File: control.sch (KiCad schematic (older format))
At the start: 17 parts, among them IC1 ATTINY4313-P, P2 CONN_02X03, SW1 SW_Push, Y1 11.0592MHz

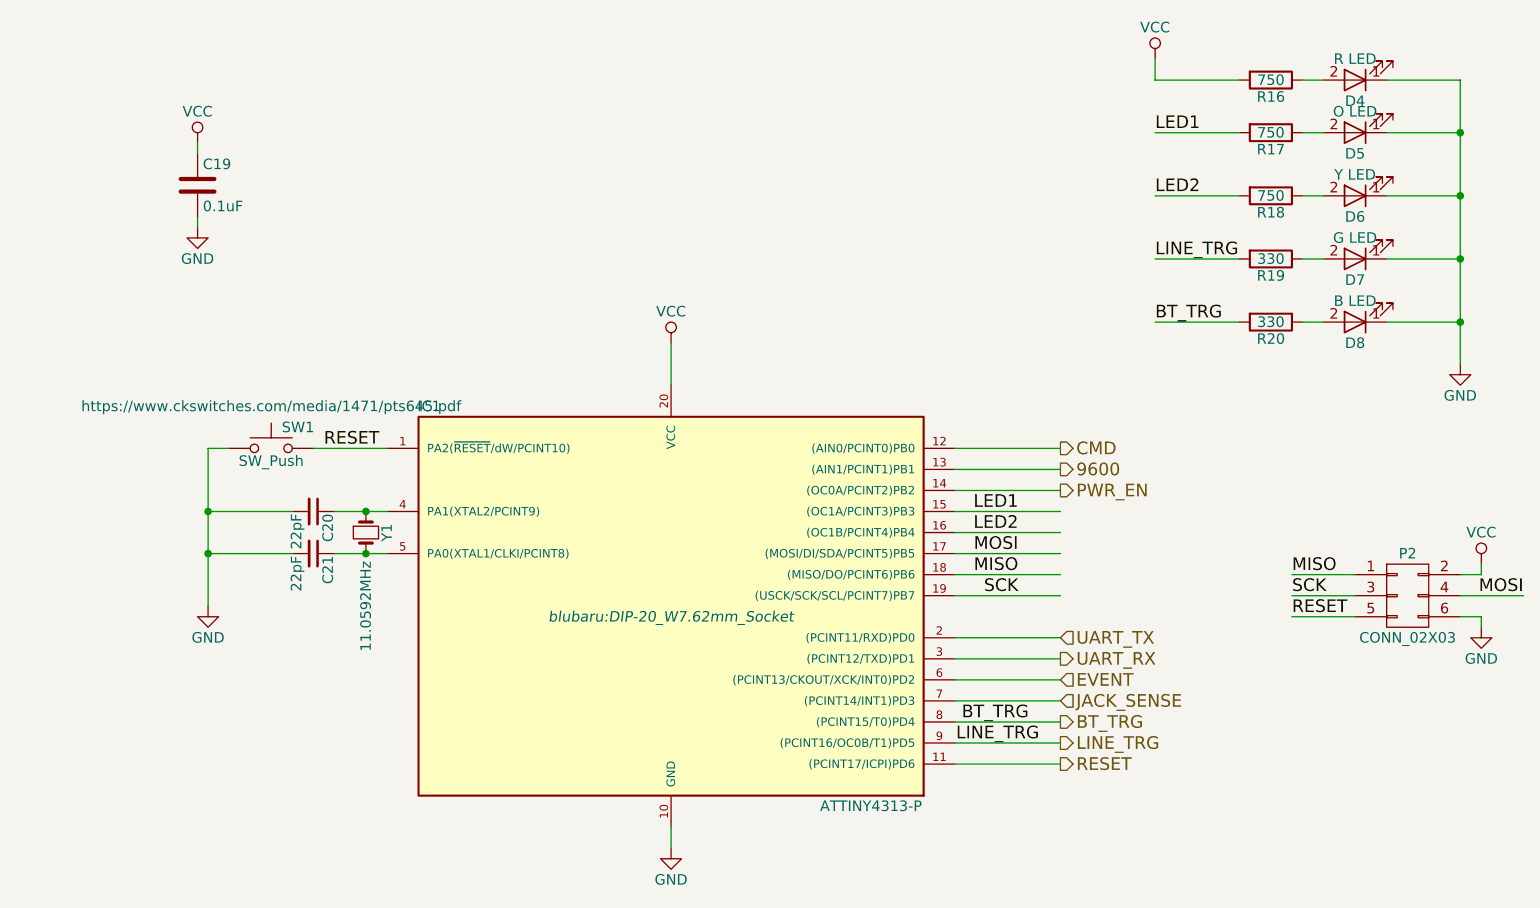
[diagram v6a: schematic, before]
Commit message: Rename the bluetooth reset line
This is needed so it doesn't conflict with the MCU reset line of the
same name. Apparently that puts them on the same net.

Also, reorder the LEDs so they have nicer numbers on the board.
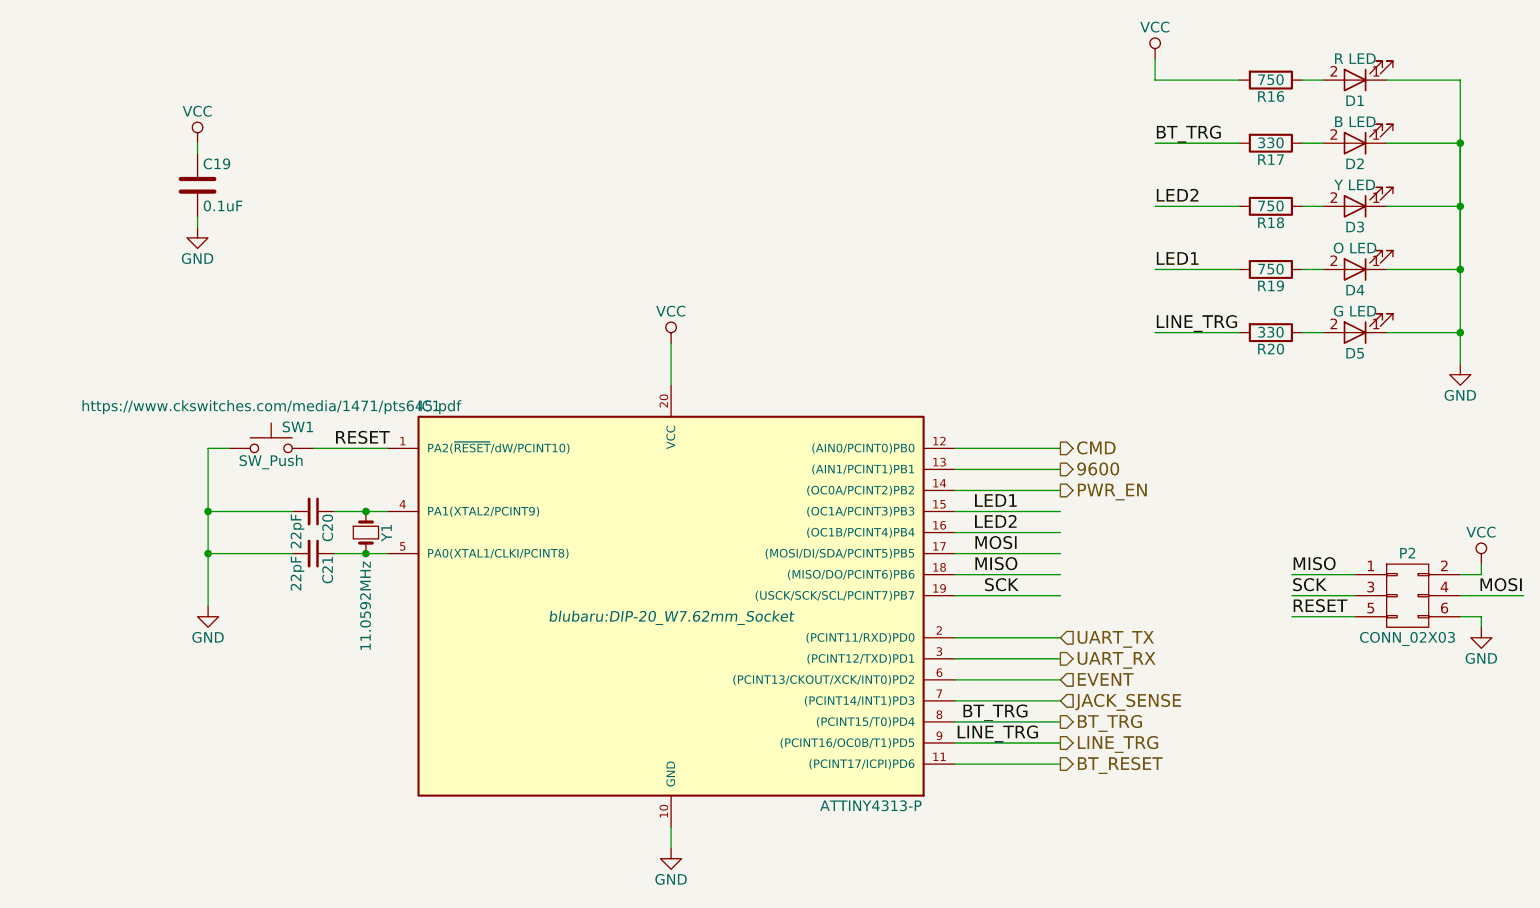
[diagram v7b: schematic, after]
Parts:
- renumbered D4 to D1, D8 to D2, D6 to D3, D5 to D4, D7 to D5, R20 to R17, R17 to R19, R19 to R20
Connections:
- net labels added: BT_RESET
- wire segments 51 -> 52
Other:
- moved on the sheet: D2, D3, D4, D5, R17, R18, R19, R20

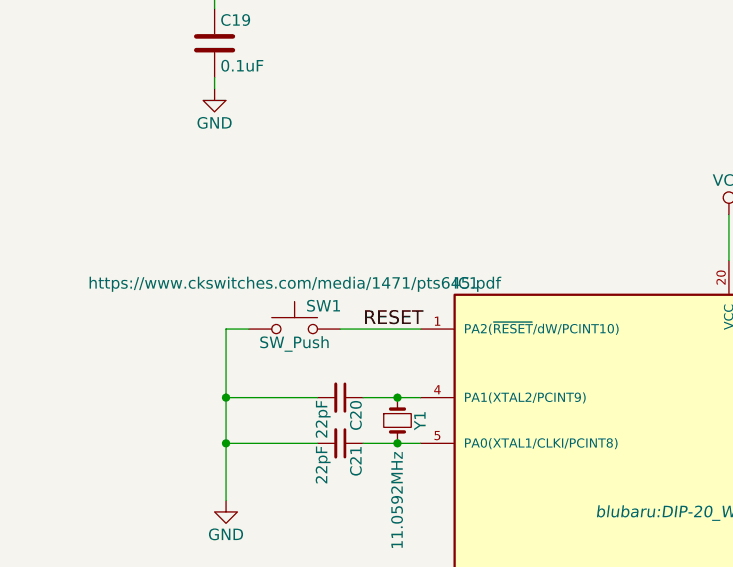
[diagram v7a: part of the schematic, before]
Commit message: jbebels attempt at routing
All power and audio is routed, as is the crystal and UART lines. Other
digital lines remain, and the resistors for the LEDs are moved off-board
until I figure out the best place for them.

This also required a small fix to the schematic. A junction was missing,
causing the audio grounds to not be connected to the cd/stereo audio
ground.
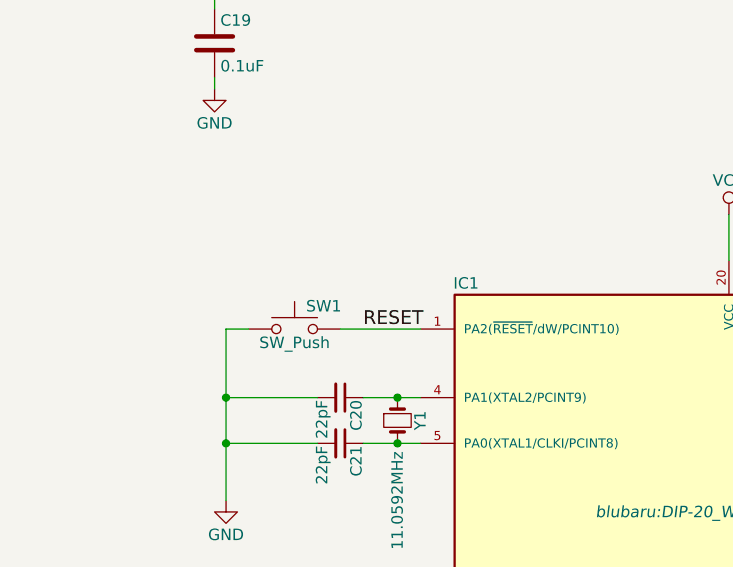
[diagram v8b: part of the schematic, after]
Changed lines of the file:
@@
 F 1 "SW_Push" H 3050 3840 50  0000 C CNN
 F 2 "blubaru:SW_Tactile_SPST_Angled_PTS645Vx58-2LFS" H 3050 4100 50  0001 C CNN
-F 3 "https://www.ckswitches.com/media/1471/pts645.pdf" H 3050 4100 50  0000 C CNN
+F 3 "https://www.ckswitches.com/media/1471/pts645.pdf" H 3050 4100 50  0001 C CNN
 	1    3050 3900
 	1    0    0    -1
